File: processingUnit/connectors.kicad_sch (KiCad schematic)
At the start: 11 parts, among them J101 +12V, J102 Conn_01x05, J103 Conn_01x04, J104 Conn_01x04

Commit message: yes
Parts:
- gave numbers to parts that had none: 1
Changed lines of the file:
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@@
 		(dnp no)
 		(fields_autoplaced yes)
-		(property "Reference" "J?"
+		(property "Reference" "J302"
 			(at 41.91 142.24 0)
 			(effects
@@
 			(project ""
 				(path "/1b1408da-cc6a-469f-a506-e797247b3ac8/26fa24e2-dd9a-49a9-9a0e-c48ef9d66c8d"
-					(reference "J?")
+					(reference "J302")
 					(unit 1)
 				)

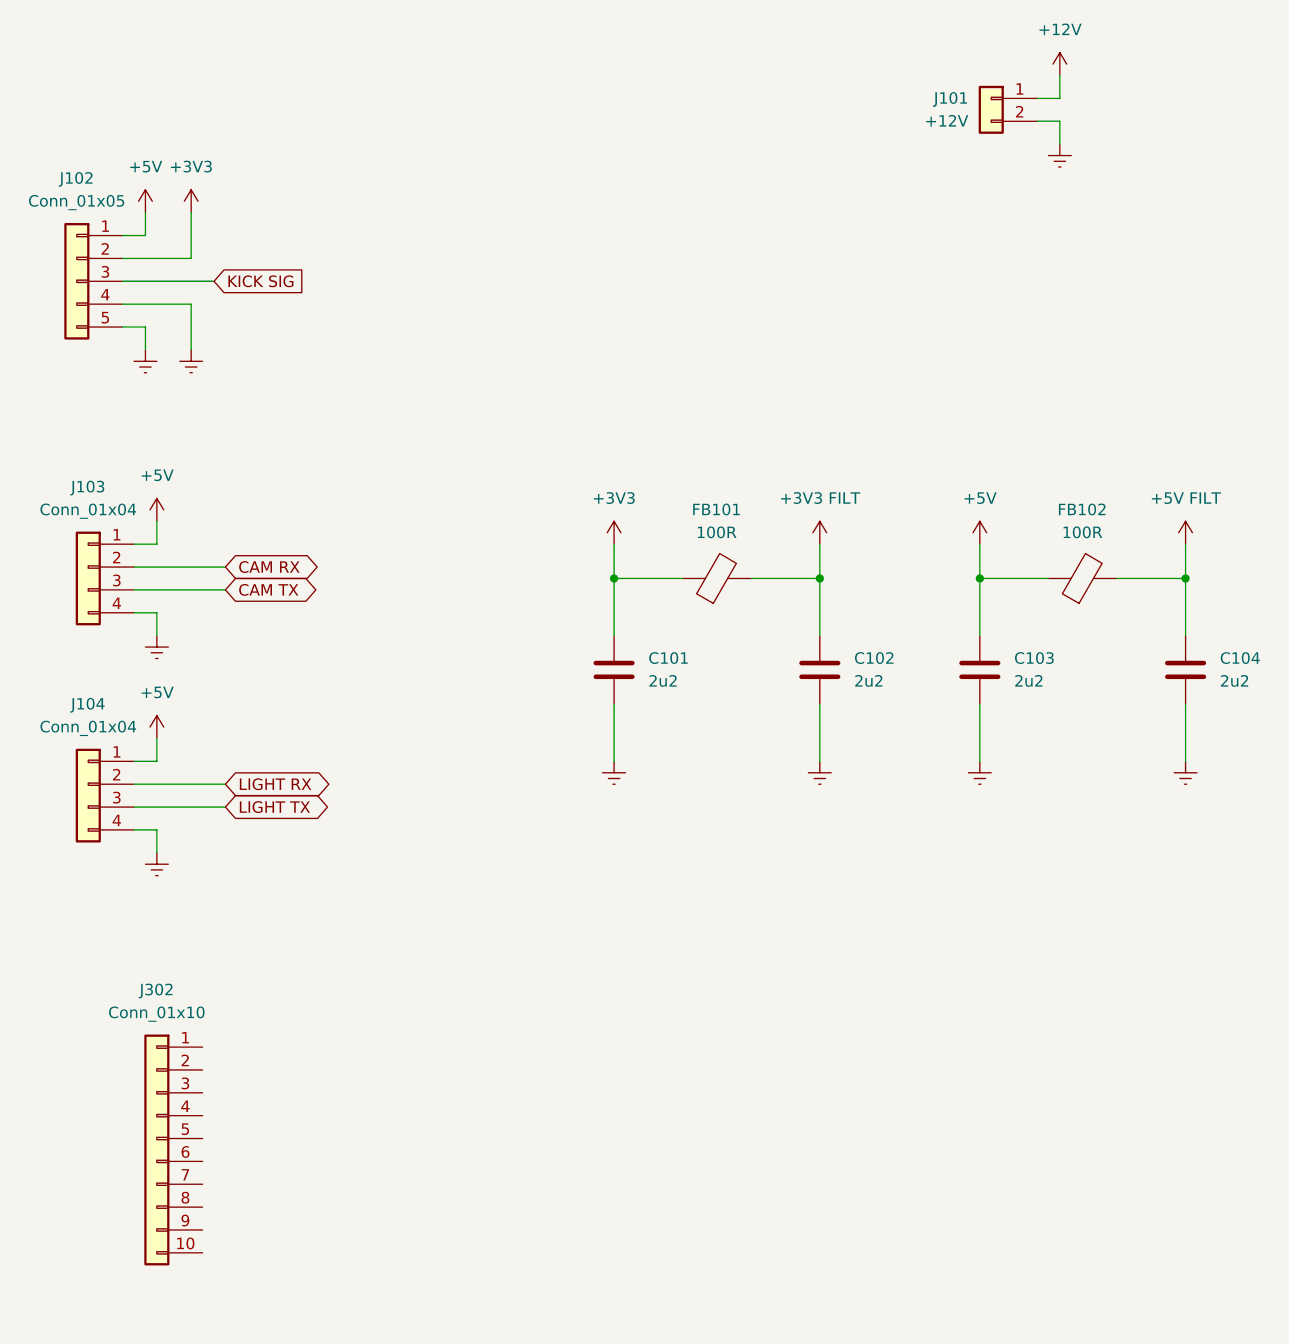
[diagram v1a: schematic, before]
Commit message: modified motor driver removed topInterface
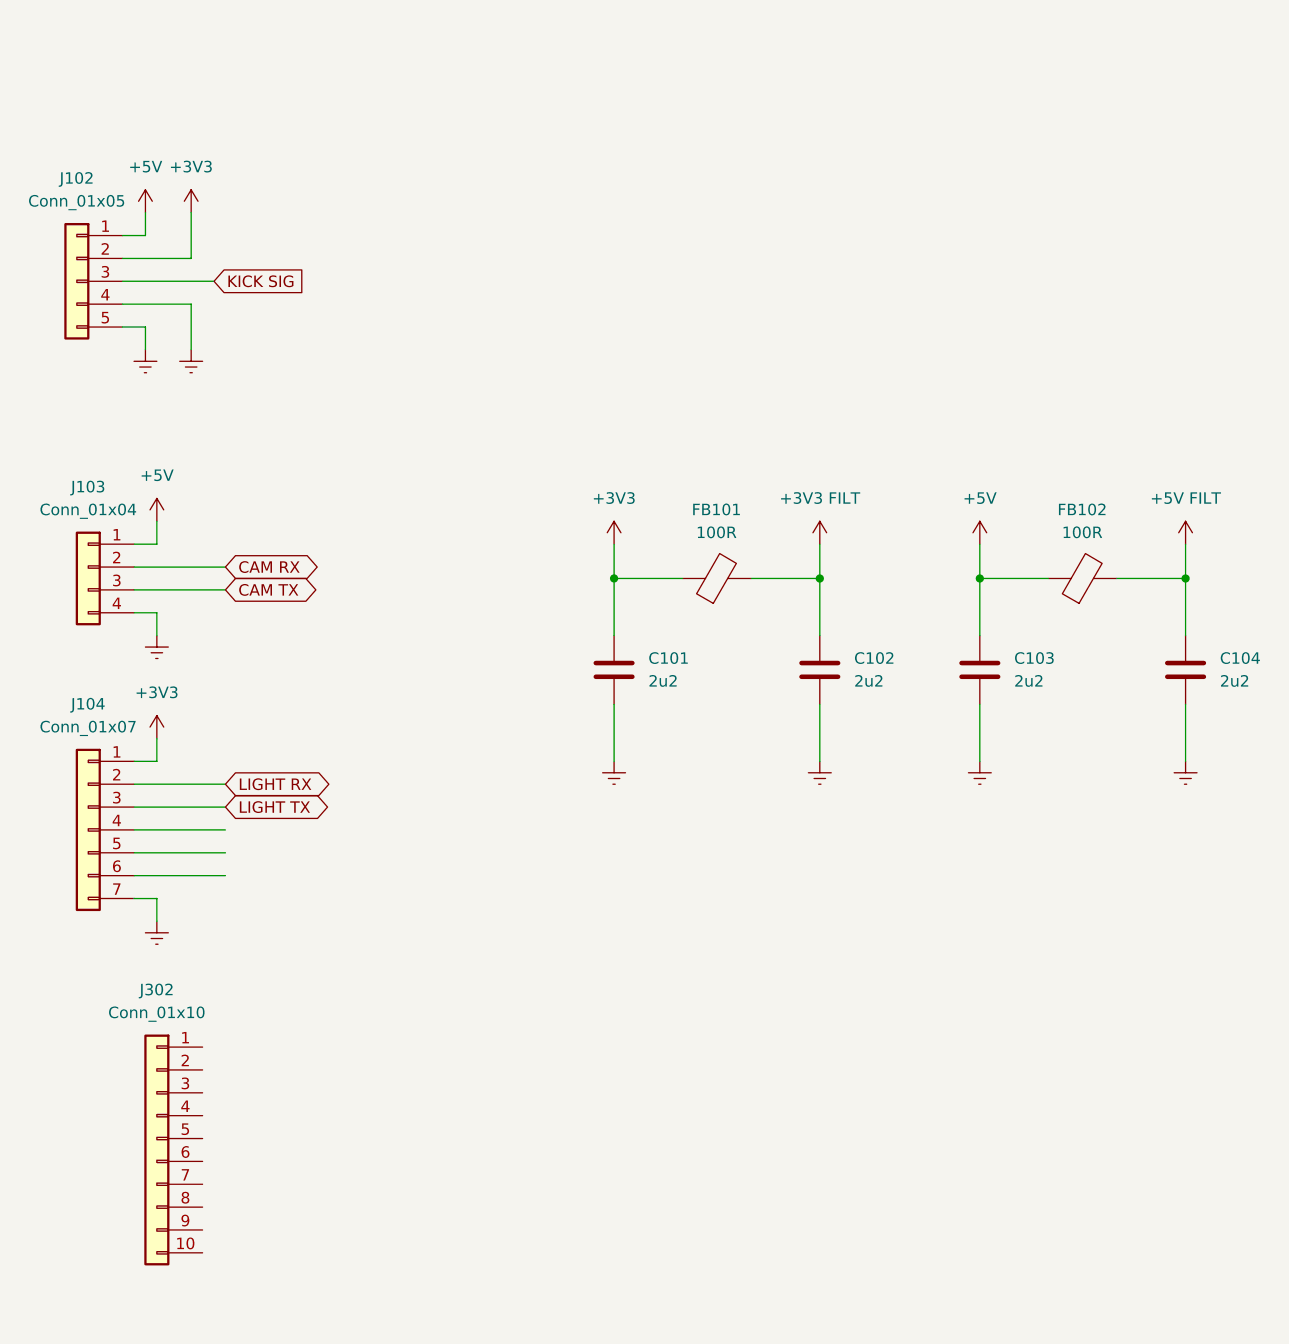
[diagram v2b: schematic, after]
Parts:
- removed J101: +12V, Library:xt30-f, symbol Connector_Generic:Conn_01x02
- removed J104: Conn_01x04, Connector_JST:JST_XH_B4B-XH-A_1x04_P2.50mm_Vertical, symbol Connector_Generic:Conn_01x04
- added J104: Conn_01x07, Connector_JST:JST_XH_S7B-XH-A_1x07_P2.50mm_Horizontal, symbol Connector_Generic:Conn_01x07
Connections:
- net +3V3: now also J104.1 (Pin_1)
- net GNDREF: now also J104.7 (Pin_7)
- net LIGHT RX: now also J104.2 (Pin_2)
- net LIGHT TX: now also J104.3 (Pin_3)

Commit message: 死
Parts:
- renumbered J102 to J101, J103 to J102, J104 to J103, J302 to J104
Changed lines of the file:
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@@
 		(dnp no)
 		(fields_autoplaced yes)
-		(property "Reference" "#PWR0308"
+		(property "Reference" "#PWR0111"
 			(at 41.91 118.11 0)
 			(effects
@@
 			(project ""
 				(path "/1b1408da-cc6a-469f-a506-e797247b3ac8/26fa24e2-dd9a-49a9-9a0e-c48ef9d66c8d"
-					(reference "#PWR0308")
+					(reference "#PWR0111")
 					(unit 1)
 				)
@@
 		(dnp no)
 		(fields_autoplaced yes)
-		(property "Reference" "#PWR0109"
+		(property "Reference" "#PWR0107"
 			(at 115.57 96.52 0)
 			(effects
@@
 			(project "l3"
 				(path "/1b1408da-cc6a-469f-a506-e797247b3ac8/26fa24e2-dd9a-49a9-9a0e-c48ef9d66c8d"
-					(reference "#PWR0109")
+					(reference "#PWR0107")
 					(unit 1)
 				)
@@
 		(dnp no)
 		(fields_autoplaced yes)
-		(property "Reference" "#PWR0108"
+		(property "Reference" "#PWR0106"
 			(at 92.71 96.52 0)
 			(effects
@@
 			(project "l3"
 				(path "/1b1408da-cc6a-469f-a506-e797247b3ac8/26fa24e2-dd9a-49a9-9a0e-c48ef9d66c8d"
-					(reference "#PWR0108")
+					(reference "#PWR0106")
 					(unit 1)
 				)
@@
 		(dnp no)
 		(fields_autoplaced yes)
-		(property "Reference" "#PWR0113"
+		(property "Reference" "#PWR0112"
 			(at 92.71 123.19 0)
 			(effects
@@
 			(project "l3"
 				(path "/1b1408da-cc6a-469f-a506-e797247b3ac8/26fa24e2-dd9a-49a9-9a0e-c48ef9d66c8d"
-					(reference "#PWR0113")
+					(reference "#PWR0112")
 					(unit 1)
 				)
@@
 		(dnp no)
 		(fields_autoplaced yes)
-		(property "Reference" "J302"
+		(property "Reference" "J104"
 			(at 41.91 142.24 0)
 			(effects
@@
 			(project ""
 				(path "/1b1408da-cc6a-469f-a506-e797247b3ac8/26fa24e2-dd9a-49a9-9a0e-c48ef9d66c8d"
-					(reference "J302")
+					(reference "J104")
 					(unit 1)
 				)
@@
 		(dnp no)
 		(fields_autoplaced yes)
-		(property "Reference" "#PWR0115"
+		(property "Reference" "#PWR0114"
 			(at 133.35 123.19 0)
 			(effects
@@
 			(project "l3"
 				(path "/1b1408da-cc6a-469f-a506-e797247b3ac8/26fa24e2-dd9a-49a9-9a0e-c48ef9d66c8d"
-					(reference "#PWR0115")
+					(reference "#PWR0114")
 					(unit 1)
 				)
@@
 		(dnp no)
 		(fields_autoplaced yes)
-		(property "Reference" "#PWR0116"
+		(property "Reference" "#PWR0115"
 			(at 156.21 123.19 0)
 			(effects
@@
 			(project "l3"
 				(path "/1b1408da-cc6a-469f-a506-e797247b3ac8/26fa24e2-dd9a-49a9-9a0e-c48ef9d66c8d"
-					(reference "#PWR0116")
+					(reference "#PWR0115")
 					(unit 1)
 				)
@@
 		(dnp no)
 		(fields_autoplaced yes)
-		(property "Reference" "J102"
+		(property "Reference" "J101"
 			(at 33.02 52.07 0)
 			(effects
@@
 			(project ""
 				(path "/1b1408da-cc6a-469f-a506-e797247b3ac8/26fa24e2-dd9a-49a9-9a0e-c48ef9d66c8d"
-					(reference "J102")
+					(reference "J101")
 					(unit 1)
 				)
@@
 		(dnp no)
 		(fields_autoplaced yes)
-		(property "Reference" "#PWR0309"
+		(property "Reference" "#PWR0116"
 			(at 41.91 140.97 0)
 			(effects
@@
 			(project "l3"
 				(path "/1b1408da-cc6a-469f-a506-e797247b3ac8/26fa24e2-dd9a-49a9-9a0e-c48ef9d66c8d"
-					(reference "#PWR0309")
+					(reference "#PWR0116")
 					(unit 1)
 				)
@@
 		(dnp no)
 		(fields_autoplaced yes)
-		(property "Reference" "#PWR0107"
+		(property "Reference" "#PWR0105"
 			(at 41.91 93.98 0)
 			(effects
@@
 			(project "l3"
 				(path "/1b1408da-cc6a-469f-a506-e797247b3ac8/26fa24e2-dd9a-49a9-9a0e-c48ef9d66c8d"
-					(reference "#PWR0107")
+					(reference "#PWR0105")
 					(unit 1)
 				)
@@
 		(dnp no)
 		(fields_autoplaced yes)
-		(property "Reference" "#PWR0105"
+		(property "Reference" "#PWR0103"
 			(at 40.64 77.47 0)
 			(effects
@@
 			(project ""
 				(path "/1b1408da-cc6a-469f-a506-e797247b3ac8/26fa24e2-dd9a-49a9-9a0e-c48ef9d66c8d"
-					(reference "#PWR0105")
+					(reference "#PWR0103")
 					(unit 1)
 				)
@@
 		(dnp no)
 		(fields_autoplaced yes)
-		(property "Reference" "#PWR0111"
+		(property "Reference" "#PWR0109"
 			(at 156.21 96.52 0)
 			(effects
@@
 			(project "l3"
 				(path "/1b1408da-cc6a-469f-a506-e797247b3ac8/26fa24e2-dd9a-49a9-9a0e-c48ef9d66c8d"
-					(reference "#PWR0111")
+					(reference "#PWR0109")
 					(unit 1)
 				)
@@
 		(dnp no)
 		(fields_autoplaced yes)
-		(property "Reference" "#PWR0110"
+		(property "Reference" "#PWR0108"
 			(at 133.35 96.52 0)
 			(effects
@@
 			(project ""
 				(path "/1b1408da-cc6a-469f-a506-e797247b3ac8/26fa24e2-dd9a-49a9-9a0e-c48ef9d66c8d"
-					(reference "#PWR0110")
+					(reference "#PWR0108")
 					(unit 1)
 				)
@@
 		(dnp no)
 		(fields_autoplaced yes)
-		(property "Reference" "#PWR0103"
+		(property "Reference" "#PWR0101"
 			(at 40.64 59.69 0)
 			(effects
@@
 			(project ""
 				(path "/1b1408da-cc6a-469f-a506-e797247b3ac8/26fa24e2-dd9a-49a9-9a0e-c48ef9d66c8d"
-					(reference "#PWR0103")
+					(reference "#PWR0101")
 					(unit 1)
 				)
@@
 		(dnp no)
 		(fields_autoplaced yes)
-		(property "Reference" "#PWR0106"
+		(property "Reference" "#PWR0104"
 			(at 45.72 77.47 0)
 			(effects
@@
 			(project ""
 				(path "/1b1408da-cc6a-469f-a506-e797247b3ac8/26fa24e2-dd9a-49a9-9a0e-c48ef9d66c8d"
-					(reference "#PWR0106")
+					(reference "#PWR0104")
 					(unit 1)
 				)
@@
 		(dnp no)
 		(fields_autoplaced yes)
-		(property "Reference" "J104"
+		(property "Reference" "J103"
 			(at 34.29 110.49 0)
 			(effects
@@
 			(project ""
 				(path "/1b1408da-cc6a-469f-a506-e797247b3ac8/26fa24e2-dd9a-49a9-9a0e-c48ef9d66c8d"
-					(reference "J104")
+					(reference "J103")
 					(unit 1)
 				)
@@
 		(dnp no)
 		(fields_autoplaced yes)
-		(property "Reference" "#PWR0114"
+		(property "Reference" "#PWR0113"
 			(at 115.57 123.19 0)
 			(effects
@@
 			(project "l3"
 				(path "/1b1408da-cc6a-469f-a506-e797247b3ac8/26fa24e2-dd9a-49a9-9a0e-c48ef9d66c8d"
-					(reference "#PWR0114")
+					(reference "#PWR0113")
 					(unit 1)
 				)
@@
 		(dnp no)
 		(fields_autoplaced yes)
-		(property "Reference" "#PWR0112"
+		(property "Reference" "#PWR0110"
 			(at 41.91 109.22 0)
 			(effects
@@
 			(project "l3"
 				(path "/1b1408da-cc6a-469f-a506-e797247b3ac8/26fa24e2-dd9a-49a9-9a0e-c48ef9d66c8d"
-					(reference "#PWR0112")
+					(reference "#PWR0110")
 					(unit 1)
 				)
@@
 		(dnp no)
 		(fields_autoplaced yes)
-		(property "Reference" "J103"
+		(property "Reference" "J102"
 			(at 34.29 86.36 0)
 			(effects
@@
 			(project ""
 				(path "/1b1408da-cc6a-469f-a506-e797247b3ac8/26fa24e2-dd9a-49a9-9a0e-c48ef9d66c8d"
-					(reference "J103")
+					(reference "J102")
 					(unit 1)
 				)
@@
 		(dnp no)
 		(fields_autoplaced yes)
-		(property "Reference" "#PWR0104"
+		(property "Reference" "#PWR0102"
 			(at 45.72 59.69 0)
 			(effects
@@
 			(project ""
 				(path "/1b1408da-cc6a-469f-a506-e797247b3ac8/26fa24e2-dd9a-49a9-9a0e-c48ef9d66c8d"
-					(reference "#PWR0104")
-					(unit 1)
-				)
+					(reference "#PWR0102")
+					(unit 1)
+				)

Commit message: L3 Schematic
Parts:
- removed J103: Conn_01x07, Connector_JST:JST_XH_S7B-XH-A_1x07_P2.50mm_Horizontal, symbol Connector_Generic:Conn_01x07
- added J301: Conn_01x10, Library:526101071, symbol Connector_Generic:Conn_01x10
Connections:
- net +3V3: now also J301.1 (Pin_1)
- net GNDREF: now also J301.10 (Pin_10)
- net LIGHT RX: now also J301.3 (Pin_3)
- net LIGHT TX: now also J301.4 (Pin_4)
- new net MCU RST: J301.5 (Pin_5)
- new net MCU SWCLK: J301.7 (Pin_7)
- new net MCU SWDIO: J301.6 (Pin_6)
- no-connect marks 0 -> 3

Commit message: Schematic L3
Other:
- moved on the sheet: J104
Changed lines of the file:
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@@
 	(symbol
 		(lib_id "Connector_Generic:Conn_01x10")
-		(at 41.91 158.75 0)
+		(at 67.7328 165.5299 0)
 		(mirror y)
 		(unit 1)
@@
 		(fields_autoplaced yes)
 		(property "Reference" "J104"
-			(at 41.91 142.24 0)
+			(at 67.7328 149.0199 0)
 			(effects
 				(font
@@
 		)
 		(property "Value" "Conn_01x10"
-			(at 41.91 144.78 0)
+			(at 67.7328 151.5599 0)
 			(effects
 				(font
@@
 		)
 		(property "Footprint" ""
-			(at 41.91 158.75 0)
+			(at 67.7328 165.5299 0)
 			(effects
 				(font
@@
 		)
 		(property "Datasheet" "~"
-			(at 41.91 158.75 0)
+			(at 67.7328 165.5299 0)
 			(effects
 				(font
@@
 		)
 		(property "Description" "Generic connector, single row, 01x10, script generated (kicad-library-utils/schlib/autogen/connector/)"
-			(at 41.91 158.75 0)
+			(at 67.7328 165.5299 0)
 			(effects
 				(font

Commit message: footprint
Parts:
- J104: footprint (none) -> Library:526101071
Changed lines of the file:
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@@
 			)
 		)
-		(property "Footprint" ""
+		(property "Footprint" "Library:526101071"
 			(at 67.7328 165.5299 0)
 			(effects

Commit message: L3 layout
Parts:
- removed J104: Conn_01x10, Library:526101071, symbol Connector_Generic:Conn_01x10
- added J309: Conn_01x02, Library:xt30-f, symbol Connector_Generic:Conn_01x02
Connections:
- net GNDREF: now also J309.1 (Pin_1)
- new net +12V: J309.2 (Pin_2)
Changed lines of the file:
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@@
+	(wire
+		(pts
+			(xy 59.69 152.4) (xy 55.88 152.4)
+		)
+		(stroke
+			(width 0)
+			(type default)
+		)
+	)
 	(wire
 		(pts
@@
 	)
 	(symbol
+		(lib_id "power:+12V")
+		(at 59.69 152.4 0)
+		(unit 1)
+		(exclude_from_sim no)
+		(in_bom yes)
+		(on_board yes)
+		(dnp no)
+		(fields_autoplaced yes)
+		(property "Reference" "#PWR0353"
+			(at 59.69 156.21 0)
+			(effects
+				(font
+					(size 1.27 1.27)
+				)
+				(hide yes)
+			)
+		)
+		(property "Value" "+12V"
+			(at 59.69 147.32 0)
+			(effects
+				(font
+					(size 1.27 1.27)
+				)
+			)
+		)
+		(property "Footprint" ""
+			(at 59.69 152.4 0)
+			(effects
+				(font
+					(size 1.27 1.27)
+				)
+				(hide yes)
+			)
+		)
+		(property "Datasheet" ""
+			(at 59.69 152.4 0)
+			(effects
+				(font
+					(size 1.27 1.27)
+				)
+				(hide yes)
+			)
+		)
+		(property "Description" "Power symbol creates a global label with name \"+12V\""
+			(at 59.69 152.4 0)
+			(effects
+				(font
+					(size 1.27 1.27)
+				)
+				(hide yes)
+			)
+		)
+		(pin "1"
+		)
+		(instances
+			(project "l3"
+				(path "/1b1408da-cc6a-469f-a506-e797247b3ac8/26fa24e2-dd9a-49a9-9a0e-c48ef9d66c8d"
+					(reference "#PWR0353")
+					(unit 1)
+				)
+			)
+		)
+	)
+	(symbol
 		(lib_id "power:+3V3")
 		(at 115.57 92.71 0)
@@
 				(path "/1b1408da-cc6a-469f-a506-e797247b3ac8/26fa24e2-dd9a-49a9-9a0e-c48ef9d66c8d"
 					(reference "#PWR0319")
-					(unit 1)
-				)
-			)
-		)
-	)
-	(symbol
-		(lib_id "Connector_Generic:Conn_01x10")
-		(at 67.7328 165.5299 0)
-		(mirror y)
-		(unit 1)
-		(exclude_from_sim no)
-		(in_bom yes)
-		(on_board yes)
-		(dnp no)
-		(fields_autoplaced yes)
-		(property "Reference" "J104"
-			(at 67.7328 149.0199 0)
-			(effects
-				(font
-					(size 1.27 1.27)
-				)
-			)
-		)
-		(property "Value" "Conn_01x10"
-			(at 67.7328 151.5599 0)
-			(effects
-				(font
-					(size 1.27 1.27)
-				)
-			)
-		)
-		(property "Footprint" "Library:526101071"
-			(at 67.7328 165.5299 0)
-			(effects
-				(font
-					(size 1.27 1.27)
-				)
-				(hide yes)
-			)
-		)
-		(property "Datasheet" "~"
-			(at 67.7328 165.5299 0)
-			(effects
-				(font
-					(size 1.27 1.27)
-				)
-				(hide yes)
-			)
-		)
-		(property "Description" "Generic connector, single row, 01x10, script generated (kicad-library-utils/schlib/autogen/connector/)"
-			(at 67.7328 165.5299 0)
-			(effects
-				(font
-					(size 1.27 1.27)
-				)
-				(hide yes)
-			)
-		)
-		(pin "3"
-		)
-		(pin "2"
-		)
-		(pin "9"
-		)
-		(pin "4"
-		)
-		(pin "7"
-		)
-		(pin "8"
-		)
-		(pin "6"
-		)
-		(pin "5"
-		)
-		(pin "1"
-		)
-		(pin "10"
-		)
-		(instances
-			(project "l3"
-				(path "/1b1408da-cc6a-469f-a506-e797247b3ac8/26fa24e2-dd9a-49a9-9a0e-c48ef9d66c8d"
-					(reference "J104")
 					(unit 1)
 				)
@@
 					(unit 1)
 				)
+			)
+		)
+	)
+	(symbol
+		(lib_id "Connector_Generic:Conn_01x02")
+		(at 50.8 154.94 180)
+		(unit 1)
+		(exclude_from_sim no)
+		(in_bom yes)
+		(on_board yes)
+		(dnp no)
+		(fields_autoplaced yes)
+		(property "Reference" "J309"
+			(at 50.8 146.05 0)
+			(effects
+				(font
+					(size 1.27 1.27)
+				)
+			)
+		)
+		(property "Value" "Conn_01x02"
+			(at 50.8 148.59 0)
+			(effects
+				(font
+					(size 1.27 1.27)
+				)
+			)
+		)
+		(property "Footprint" "Library:xt30-f"
+			(at 50.8 154.94 0)
+			(effects
+				(font
+					(size 1.27 1.27)
+				)
+				(hide yes)
+			)
+		)
+		(property "Datasheet" "~"
+			(at 50.8 154.94 0)
+			(effects
+				(font
+					(size 1.27 1.27)
+				)
+				(hide yes)
+			)
+		)
+		(property "Description" "Generic connector, single row, 01x02, script generated (kicad-library-utils/schlib/autogen/connector/)"
+			(at 50.8 154.94 0)
+			(effects
+				(font
+					(size 1.27 1.27)
+				)
+				(hide yes)
+			)
+		)
+		(pin "1"
+		)
+		(pin "2"
+		)
+		(instances
+			(project "l3"
+				(path "/1b1408da-cc6a-469f-a506-e797247b3ac8/26fa24e2-dd9a-49a9-9a0e-c48ef9d66c8d"
+					(reference "J309")
+					(unit 1)
+				)
+			)
+		)
+	)
+	(symbol
+		(lib_id "power:GNDREF")
+		(at 55.88 154.94 0)
+		(unit 1)
+		(exclude_from_sim no)
+		(in_bom yes)
+		(on_board yes)
+		(dnp no)
+		(fields_autoplaced yes)
+		(property "Reference" "#PWR0354"
+			(at 55.88 161.29 0)
+			(effects
+				(font
+					(size 1.27 1.27)
+				)
+				(hide yes)
+			)
+		)
+		(property "Value" "GNDREF"
+			(at 55.88 160.02 0)
+			(effects
+				(font
+					(size 1.27 1.27)
+				)
+				(hide yes)
+			)
+		)
+		(property "Footprint" ""
+			(at 55.88 154.94 0)
+			(effects
+				(font
+					(size 1.27 1.27)
+				)
+				(hide yes)
+			)
+		)
+		(property "Datasheet" ""
+			(at 55.88 154.94 0)
+			(effects
+				(font
+					(size 1.27 1.27)
+				)
+				(hide yes)
+			)
+		)
+		(property "Description" "Power symbol creates a global label with name \"GNDREF\" , reference supply ground"
+			(at 55.88 154.94 0)
+			(effects
+				(font
+					(size 1.27 1.27)
+				)
+				(hide yes)
+			)
+		)
+		(pin "1"
+		)
+		(instances
+			(project "l3"
+				(path "/1b1408da-cc6a-469f-a506-e797247b3ac8/26fa24e2-dd9a-49a9-9a0e-c48ef9d66c8d"
+					(reference "#PWR0354")
+					(unit 1)
+				)

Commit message: L3
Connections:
- net +3V3: now also J301.10 (Pin_10); no longer J301.1 (Pin_1)
- net GNDREF: now also J301.1 (Pin_1); no longer J301.10 (Pin_10)
- net LIGHT RX: now also J301.7 (Pin_7); no longer J301.3 (Pin_3)
- net LIGHT TX: now also J301.8 (Pin_8); no longer J301.4 (Pin_4)
- net MCU RST: now also J301.6 (Pin_6); no longer J301.5 (Pin_5)
- net MCU SWCLK: now also J301.4 (Pin_4); no longer J301.7 (Pin_7)
- net MCU SWDIO: now also J301.5 (Pin_5); no longer J301.6 (Pin_6)
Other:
- moved on the sheet: J301
